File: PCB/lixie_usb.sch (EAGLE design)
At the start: 5 parts, among them U2 AT90USB162-16AU

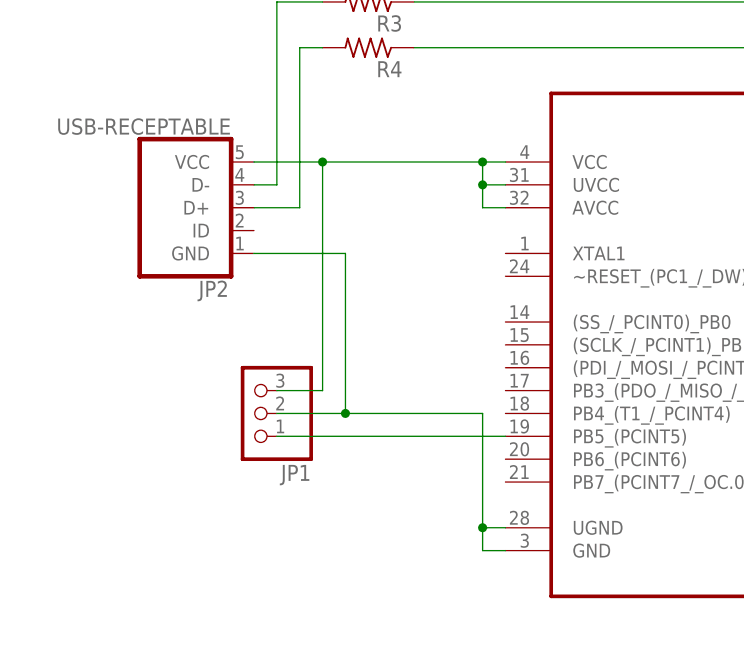
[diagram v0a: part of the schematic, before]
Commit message: Switched pin order to standard
Power/ground/data order changed to power/data/ground.
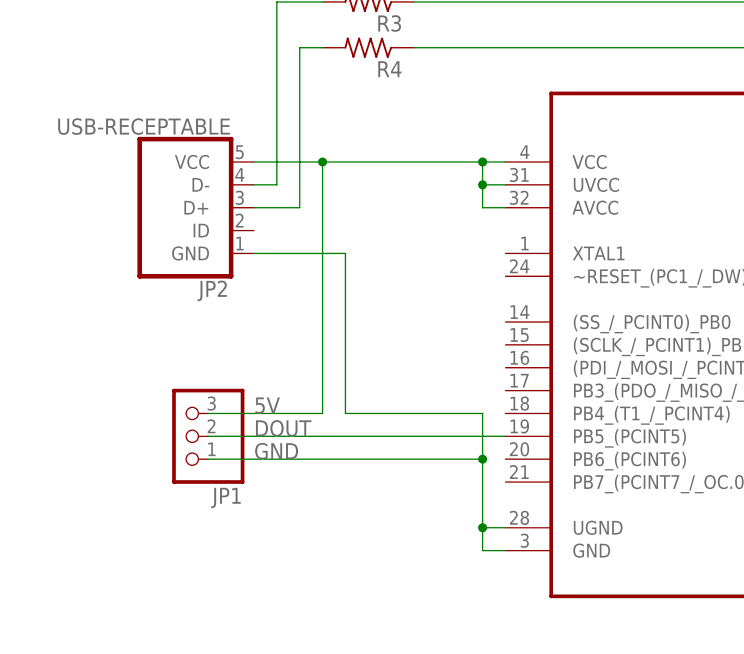
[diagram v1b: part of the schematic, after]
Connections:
- net N$20 renamed 5V
- removed net N$23: JP1.1, U2.PB5_(PCINT5)
- new net DOUT: JP1.2, U2.PB5_(PCINT5)
- net GND: now also JP1.1; no longer JP1.2
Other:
- moved on the sheet: JP1
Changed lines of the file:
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@@
 <?xml version="1.0" encoding="utf-8"?>
 <!DOCTYPE eagle SYSTEM "eagle.dtd">
-<eagle version="7.6.0">
+<eagle version="7.7.0">
 <drawing>
 <settings>
@@
 </plain>
 <instances>
-<instance part="JP1" gate="A" x="22.86" y="17.78" rot="R180"/>
+<instance part="JP1" gate="A" x="15.24" y="15.24" rot="R180"/>
 <instance part="JP2" gate="G$1" x="15.24" y="40.64" rot="R180"/>
 <instance part="U2" gate="A" x="111.76" y="27.94"/>
@@
 </busses>
 <nets>
-<net name="N$20" class="0">
-<segment>
-<wire x1="25.4" y1="20.32" x2="30.48" y2="20.32" width="0.1524" layer="91"/>
+<net name="5V" class="0">
+<segment>
+<wire x1="17.78" y1="17.78" x2="30.48" y2="17.78" width="0.1524" layer="91"/>
 <pinref part="JP1" gate="A" pin="3"/>
 <pinref part="JP2" gate="G$1" pin="VCC"/>
 <wire x1="22.86" y1="45.72" x2="30.48" y2="45.72" width="0.1524" layer="91"/>
-<wire x1="30.48" y1="45.72" x2="30.48" y2="20.32" width="0.1524" layer="91"/>
+<wire x1="30.48" y1="45.72" x2="30.48" y2="17.78" width="0.1524" layer="91"/>
 <pinref part="U2" gate="A" pin="VCC"/>
 <pinref part="U2" gate="A" pin="UVCC"/>
@@
 <wire x1="30.48" y1="45.72" x2="48.26" y2="45.72" width="0.1524" layer="91"/>
 <junction x="30.48" y="45.72"/>
+<label x="22.86" y="17.78" size="1.778" layer="95"/>
 </segment>
 </net>
 <net name="GND" class="0">
 <segment>
-<pinref part="JP1" gate="A" pin="2"/>
 <pinref part="JP2" gate="G$1" pin="GND"/>
 <wire x1="22.86" y1="35.56" x2="33.02" y2="35.56" width="0.1524" layer="91"/>
 <wire x1="33.02" y1="35.56" x2="33.02" y2="17.78" width="0.1524" layer="91"/>
-<wire x1="33.02" y1="17.78" x2="25.4" y2="17.78" width="0.1524" layer="91"/>
-<junction x="33.02" y="17.78"/>
 <pinref part="U2" gate="A" pin="UGND"/>
 <wire x1="50.8" y1="5.08" x2="48.26" y2="5.08" width="0.1524" layer="91"/>
@@
 <wire x1="50.8" y1="2.54" x2="48.26" y2="2.54" width="0.1524" layer="91"/>
 <wire x1="48.26" y1="2.54" x2="48.26" y2="5.08" width="0.1524" layer="91"/>
-<wire x1="48.26" y1="5.08" x2="48.26" y2="17.78" width="0.1524" layer="91"/>
+<wire x1="48.26" y1="5.08" x2="48.26" y2="12.7" width="0.1524" layer="91"/>
+<wire x1="48.26" y1="12.7" x2="48.26" y2="17.78" width="0.1524" layer="91"/>
 <wire x1="48.26" y1="17.78" x2="33.02" y2="17.78" width="0.1524" layer="91"/>
 <junction x="48.26" y="5.08"/>
-</segment>
-</net>
-<net name="N$23" class="0">
-<segment>
 <pinref part="JP1" gate="A" pin="1"/>
-<pinref part="U2" gate="A" pin="PB5_(PCINT5)"/>
-<wire x1="50.8" y1="15.24" x2="25.4" y2="15.24" width="0.1524" layer="91"/>
+<wire x1="17.78" y1="12.7" x2="48.26" y2="12.7" width="0.1524" layer="91"/>
+<junction x="48.26" y="12.7"/>
+<label x="22.86" y="12.7" size="1.778" layer="95"/>
 </segment>
 </net>
@@
 </segment>
 </net>
+<net name="DOUT" class="0">
+<segment>
+<pinref part="U2" gate="A" pin="PB5_(PCINT5)"/>
+<wire x1="50.8" y1="15.24" x2="17.78" y2="15.24" width="0.1524" layer="91"/>
+<pinref part="JP1" gate="A" pin="2"/>
+<label x="22.86" y="15.24" size="1.778" layer="95"/>
+</segment>
+</net>
